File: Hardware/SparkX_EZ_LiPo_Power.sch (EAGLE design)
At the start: 42 parts, among them J3 AVR_SPI_PROG_3X2TESTPOINTS, Q1 3.1A/30V/105mΩ, U1 STLQ015-3.3V, U2 MCP73831, U3 3.3V, U4 MAX17048, U5 ATTINY841-ARDUINO_QFN20M1

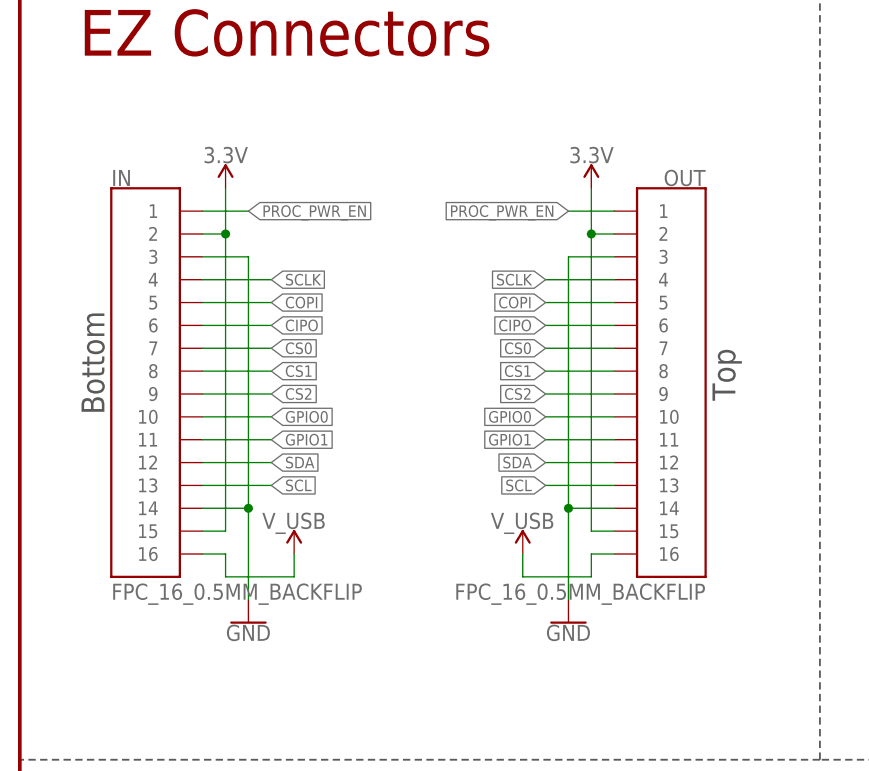
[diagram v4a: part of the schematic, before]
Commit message: Update 16-way FPC Connector. Add missing PROD_IDs
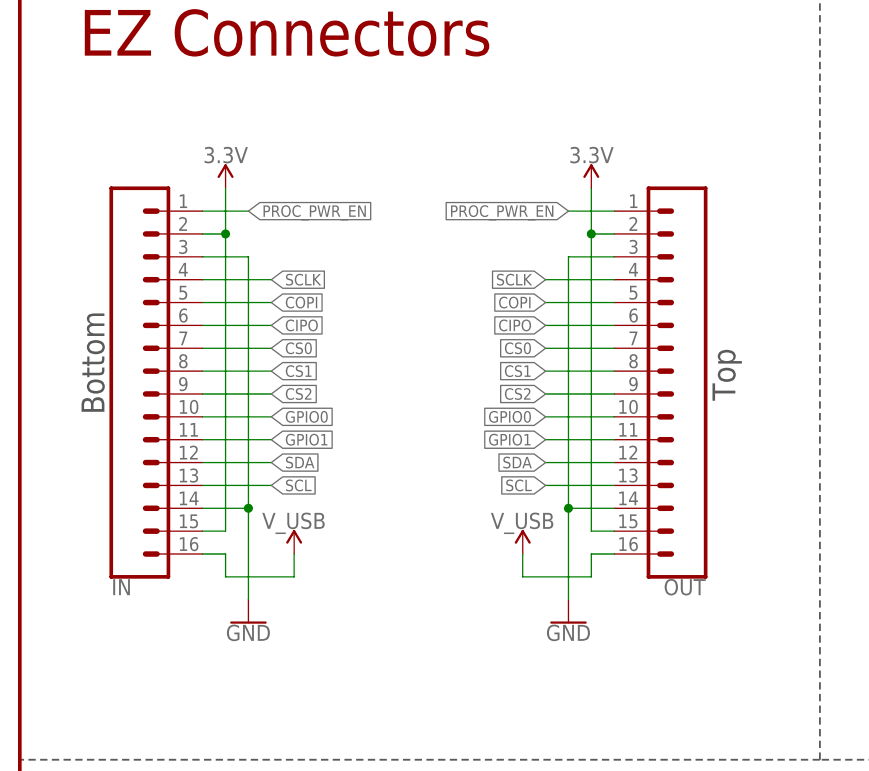
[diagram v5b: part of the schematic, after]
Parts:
- IN, OUT: value FPC_16_0.5MM_BACKFLIP -> (none); device New_Parts_Connectors:FPC_16_0.5MM_BACKFLIP -> SparkFun-Connectors:CONN_16FPC_16_0.5MM
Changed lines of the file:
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@@
 <part name="FD3" library="SparkFun-Aesthetics" deviceset="FIDUCIAL" device="UFIDUCIAL" value="FIDUCIALUFIDUCIAL"/>
 <part name="FD4" library="SparkFun-Aesthetics" deviceset="FIDUCIAL" device="UFIDUCIAL" value="FIDUCIALUFIDUCIAL"/>
-<part name="OUT" library="New_Parts_Connectors" deviceset="FPC_16_0.5MM" device="_BACKFLIP"/>
+<part name="OUT" library="SparkFun-Connectors" deviceset="CONN_16" device="FPC_16_0.5MM"/>
 <part name="SUPPLY22" library="SparkFun-PowerSymbols" deviceset="3.3V" device=""/>
 <part name="SUPPLY27" library="SparkFun-PowerSymbols" deviceset="V_USB" device=""/>
@@
 <part name="U$1" library="SparkX" deviceset="SPARKX-LOGO" device="3"/>
 <part name="LOGO3" library="SparkFun-Aesthetics" deviceset="OSHW-LOGO" device="MINI"/>
-<part name="IN" library="New_Parts_Connectors" deviceset="FPC_16_0.5MM" device="_BACKFLIP"/>
+<part name="IN" library="SparkFun-Connectors" deviceset="CONN_16" device="FPC_16_0.5MM"/>
 <part name="SUPPLY21" library="SparkFun-PowerSymbols" deviceset="3.3V" device=""/>
 <part name="SUPPLY25" library="SparkFun-PowerSymbols" deviceset="V_USB" device=""/>
@@
 <instance part="FD4" gate="G$1" x="429.26" y="27.94" smashed="yes"/>
 <instance part="LOGO2" gate="G$1" x="307.34" y="25.4" smashed="yes"/>
-<instance part="OUT" gate="G$1" x="73.66" y="233.68" smashed="yes" rot="MR0">
-<attribute name="NAME" x="76.2" y="254.254" size="1.778" layer="95" rot="MR0"/>
-<attribute name="VALUE" x="76.2" y="208.28" size="1.778" layer="96" rot="MR0"/>
+<instance part="OUT" gate="G$1" x="76.2" y="231.14" smashed="yes" rot="R180">
+<attribute name="NAME" x="76.2" y="210.566" size="1.778" layer="95" rot="R180"/>
+<attribute name="VALUE" x="78.74" y="256.54" size="1.778" layer="96" rot="R180"/>
 </instance>
 <instance part="SUPPLY22" gate="G$1" x="63.5" y="254" smashed="yes">
@@
 <instance part="U$1" gate="G$1" x="307.34" y="7.62" smashed="yes"/>
 <instance part="LOGO3" gate="G$1" x="307.34" y="25.4" smashed="yes"/>
-<instance part="IN" gate="G$1" x="12.7" y="233.68" smashed="yes">
-<attribute name="NAME" x="10.16" y="254.254" size="1.778" layer="95"/>
-<attribute name="VALUE" x="10.16" y="208.28" size="1.778" layer="96"/>
+<instance part="IN" gate="G$1" x="10.16" y="231.14" smashed="yes" rot="MR180">
+<attribute name="NAME" x="10.16" y="210.566" size="1.778" layer="95" rot="MR180"/>
+<attribute name="VALUE" x="7.62" y="256.54" size="1.778" layer="96" rot="MR180"/>
 </instance>
 <instance part="SUPPLY21" gate="G$1" x="22.86" y="254" smashed="yes">
@@
 <segment>
 <pinref part="SUPPLY22" gate="G$1" pin="3.3V"/>
-<wire x1="63.5" y1="254" x2="63.5" y2="248.92" width="0.1524" layer="91"/>
 <pinref part="OUT" gate="G$1" pin="2"/>
-<wire x1="63.5" y1="248.92" x2="66.04" y2="248.92" width="0.1524" layer="91"/>
 <pinref part="OUT" gate="G$1" pin="15"/>
 <wire x1="66.04" y1="215.9" x2="63.5" y2="215.9" width="0.1524" layer="91"/>
 <wire x1="63.5" y1="215.9" x2="63.5" y2="248.92" width="0.1524" layer="91"/>
+<wire x1="63.5" y1="248.92" x2="63.5" y2="254" width="0.1524" layer="91"/>
+<wire x1="66.04" y1="248.92" x2="63.5" y2="248.92" width="0.1524" layer="91"/>
 <junction x="63.5" y="248.92"/>
 </segment>
 <segment>
 <pinref part="SUPPLY21" gate="G$1" pin="3.3V"/>
-<wire x1="22.86" y1="254" x2="22.86" y2="248.92" width="0.1524" layer="91"/>
 <pinref part="IN" gate="G$1" pin="2"/>
-<wire x1="22.86" y1="248.92" x2="20.32" y2="248.92" width="0.1524" layer="91"/>
 <pinref part="IN" gate="G$1" pin="15"/>
 <wire x1="20.32" y1="215.9" x2="22.86" y2="215.9" width="0.1524" layer="91"/>
 <wire x1="22.86" y1="215.9" x2="22.86" y2="248.92" width="0.1524" layer="91"/>
+<wire x1="22.86" y1="248.92" x2="22.86" y2="254" width="0.1524" layer="91"/>
+<wire x1="20.32" y1="248.92" x2="22.86" y2="248.92" width="0.1524" layer="91"/>
 <junction x="22.86" y="248.92"/>
 </segment>
@@
 <pinref part="IN" gate="G$1" pin="16"/>
 <wire x1="20.32" y1="213.36" x2="22.86" y2="213.36" width="0.1524" layer="91"/>
-<wire x1="22.86" y1="210.82" x2="22.86" y2="213.36" width="0.1524" layer="91"/>
-</segment>
-<segment>
+<wire x1="22.86" y1="213.36" x2="22.86" y2="210.82" width="0.1524" layer="91"/>
+</segment>
+<segment>
